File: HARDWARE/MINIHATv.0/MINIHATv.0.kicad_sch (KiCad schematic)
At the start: 0 parts

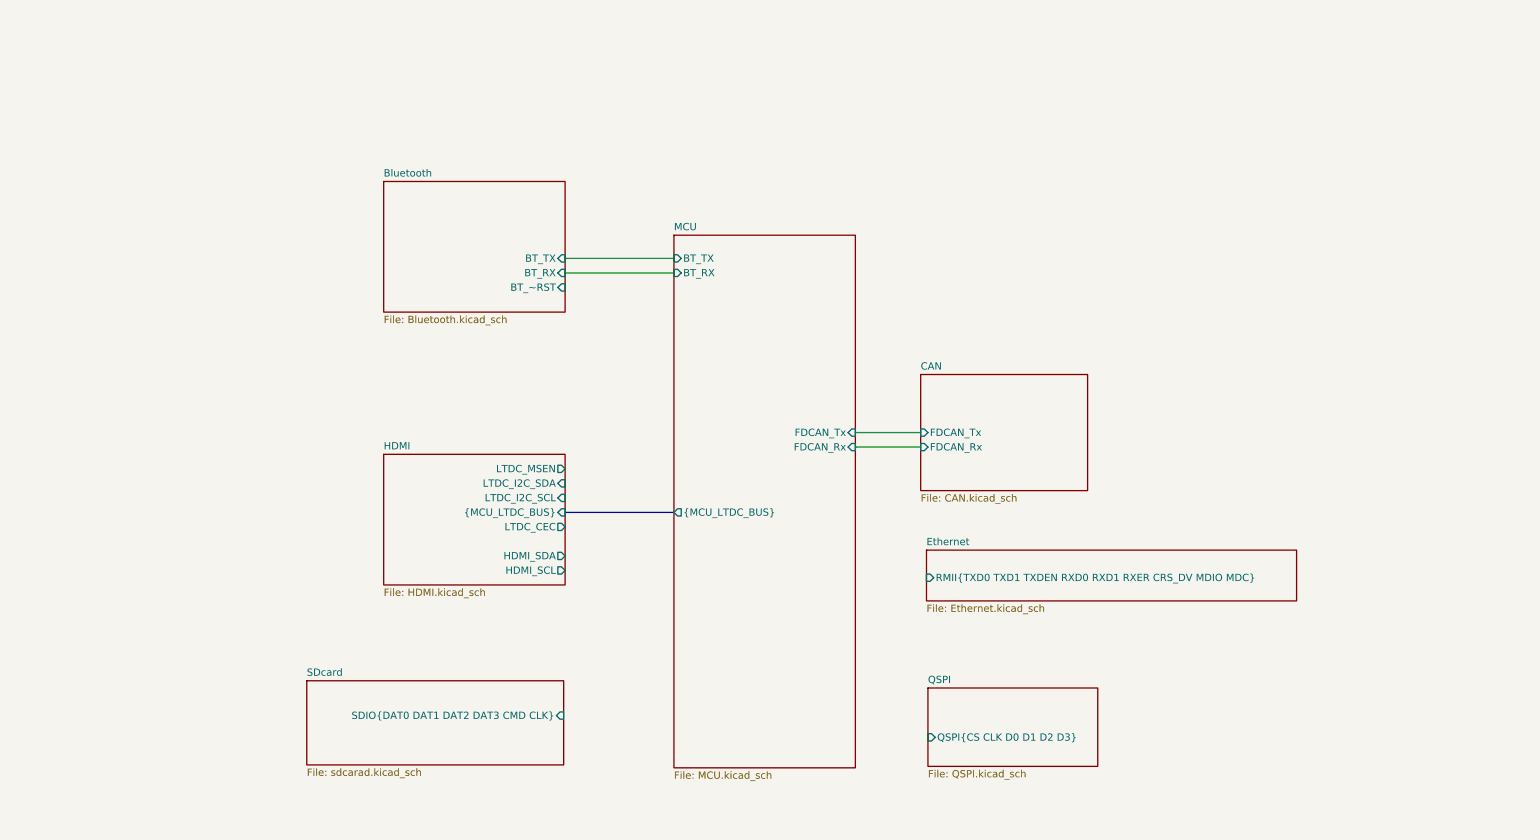
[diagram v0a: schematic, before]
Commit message: buses defined ind project settings, added stm antenna footprint, organized TOP
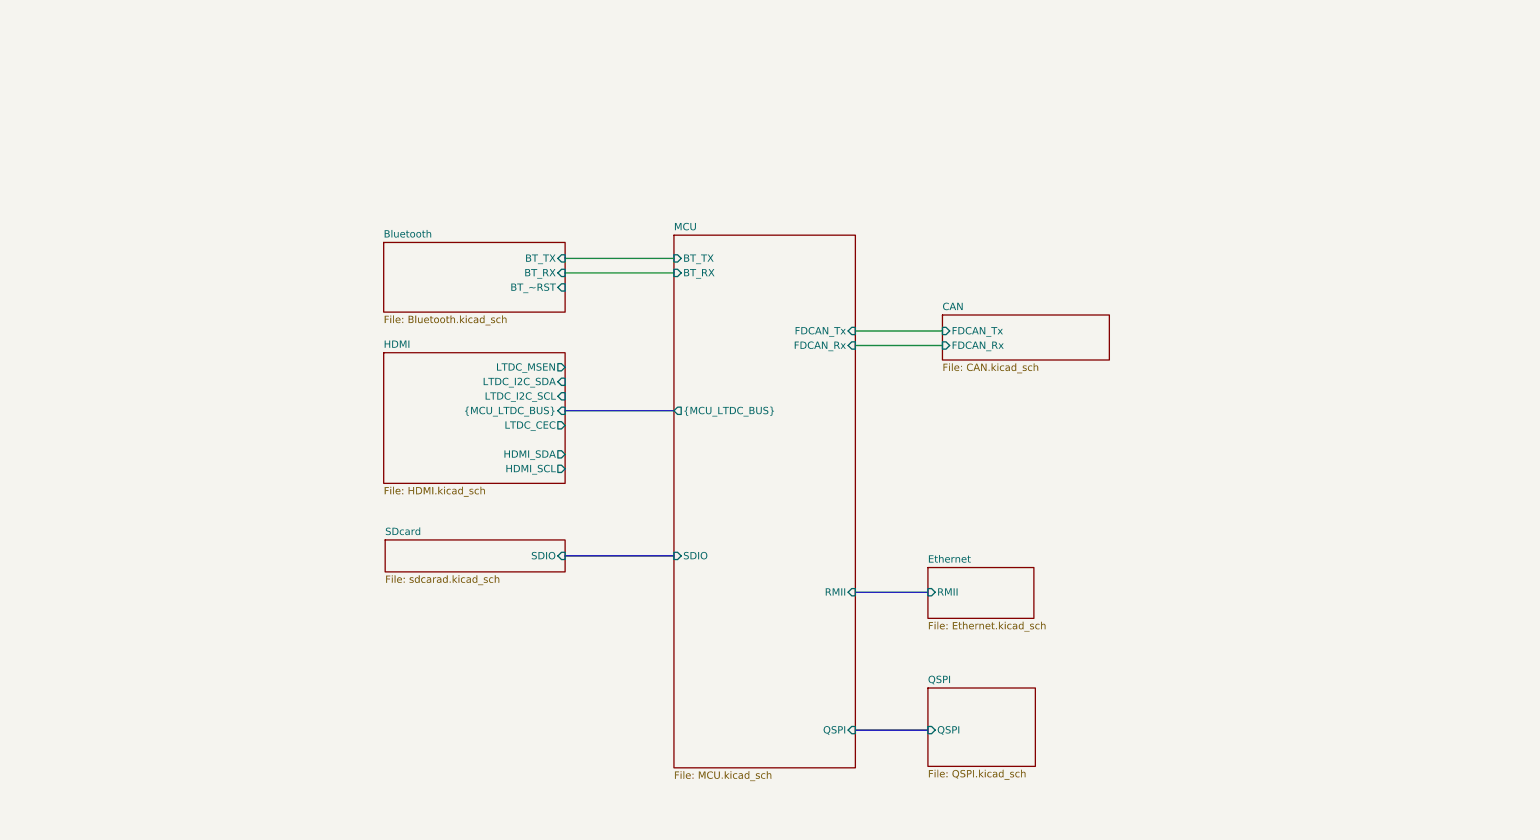
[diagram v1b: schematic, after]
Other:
- sheet Ethernet ports: added RMII; removed RMII{TXD0 TXD1 TXDEN RXD0 RXD1 RXER CRS_DV MDIO MDC}
- sheet MCU ports: added QSPI, RMII, SDIO; removed none
- sheet QSPI ports: added QSPI; removed QSPI{CS CLK D0 D1 D2 D3}
- sheet SDcard ports: added SDIO; removed SDIO{DAT0 DAT1 DAT2 DAT3 CMD CLK}
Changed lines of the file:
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@@
 	(wire
 		(pts
-			(xy 160.02 86.36) (xy 171.45 86.36)
+			(xy 160.02 68.58) (xy 175.26 68.58)
+		)
+		(stroke
+			(width 0)
+			(type default)
+		)
+	)
+	(bus
+		(pts
+			(xy 160.02 138.43) (xy 172.72 138.43)
 		)
 		(stroke
@@
 		)
 	)
+	(bus
+		(pts
+			(xy 109.22 107.95) (xy 128.27 107.95)
+		)
+		(stroke
+			(width 0)
+			(type default)
+		)
+	)
 	(wire
 		(pts
-			(xy 160.02 88.9) (xy 171.45 88.9)
+			(xy 160.02 71.12) (xy 175.26 71.12)
 		)
 		(stroke
@@
 	(bus
 		(pts
-			(xy 109.22 100.33) (xy 128.27 100.33)
-		)
-		(stroke
-			(width 0)
-			(type default)
-		)
-	)
-	(sheet
-		(at 77.47 42.418)
-		(size 31.75 22.86)
+			(xy 109.22 82.55) (xy 128.27 82.55)
+		)
+		(stroke
+			(width 0)
+			(type default)
+		)
+	)
+	(bus
+		(pts
+			(xy 160.02 114.3) (xy 172.72 114.3)
+		)
+		(stroke
+			(width 0)
+			(type default)
+		)
+	)
+	(sheet
+		(at 77.47 53.086)
+		(size 31.75 12.192)
 		(exclude_from_sim no)
 		(in_bom yes)
@@
 		)
 		(property "Sheetname" "Bluetooth"
-			(at 77.47 41.7064 0)
+			(at 77.47 52.3744 0)
 			(show_name no)
 			(do_not_autoplace no)
@@
 	)
 	(sheet
-		(at 171.45 76.2)
-		(size 29.21 20.32)
+		(at 175.26 65.786)
+		(size 29.21 7.874)
 		(exclude_from_sim no)
 		(in_bom yes)
@@
 		)
 		(property "Sheetname" "CAN"
-			(at 171.45 75.4884 0)
+			(at 175.26 65.0744 0)
 			(show_name no)
 			(do_not_autoplace no)
@@
 		)
 		(property "Sheetfile" "CAN.kicad_sch"
-			(at 171.45 97.1046 0)
+			(at 175.26 74.2446 0)
 			(show_name no)
 			(do_not_autoplace no)
@@
 		)
 		(pin "FDCAN_Rx" input
-			(at 171.45 88.9 180)
+			(at 175.26 71.12 180)
 			(effects
 				(font
@@
 		)
 		(pin "FDCAN_Tx" input
-			(at 171.45 86.36 180)
+			(at 175.26 68.58 180)
 			(effects
 				(font
@@
 	)
 	(sheet
-		(at 77.47 90.17)
+		(at 77.47 72.39)
 		(size 31.75 22.86)
 		(exclude_from_sim no)
@@
 		)
 		(property "Sheetname" "HDMI"
-			(at 77.47 89.4584 0)
+			(at 77.47 71.6784 0)
 			(show_name no)
 			(do_not_autoplace no)
@@
 		)
 		(property "Sheetfile" "HDMI.kicad_sch"
-			(at 77.47 113.6146 0)
+			(at 77.47 95.8346 0)
 			(show_name no)
 			(do_not_autoplace no)
@@
 		)
 		(pin "{MCU_LTDC_BUS}" input
-			(at 109.22 100.33 0)
+			(at 109.22 82.55 0)
 			(effects
 				(font
@@
 		)
 		(pin "HDMI_SCL" output
-			(at 109.22 110.49 0)
+			(at 109.22 92.71 0)
 			(effects
 				(font
@@
 		)
 		(pin "HDMI_SDA" output
-			(at 109.22 107.95 0)
+			(at 109.22 90.17 0)
 			(effects
 				(font
@@
 		)
 		(pin "LTDC_CEC" output
-			(at 109.22 102.87 0)
+			(at 109.22 85.09 0)
 			(effects
 				(font
@@
 		)
 		(pin "LTDC_I2C_SCL" input
-			(at 109.22 97.79 0)
+			(at 109.22 80.01 0)
 			(effects
 				(font
@@
 		)
 		(pin "LTDC_I2C_SDA" input
-			(at 109.22 95.25 0)
+			(at 109.22 77.47 0)
 			(effects
 				(font
@@
 		)
 		(pin "LTDC_MSEN" output
-			(at 109.22 92.71 0)
+			(at 109.22 74.93 0)
 			(effects
 				(font
@@
 	)
 	(sheet
-		(at 172.466 106.934)
-		(size 64.77 8.89)
+		(at 172.72 109.982)
+		(size 18.542 8.89)
 		(exclude_from_sim no)
 		(in_bom yes)
@@
 		)
 		(property "Sheetname" "Ethernet"
-			(at 172.466 106.2224 0)
+			(at 172.72 109.2704 0)
 			(show_name no)
 			(do_not_autoplace no)
@@
 		)
 		(property "Sheetfile" "Ethernet.kicad_sch"
-			(at 172.466 116.4086 0)
-			(show_name no)
-			(do_not_autoplace no)
-			(effects
-				(font
-					(size 1.27 1.27)
-				)
-				(justify left top)
-			)
-		)
-		(pin "RMII{TXD0 TXD1 TXDEN RXD0 RXD1 RXER CRS_DV MDIO MDC}" input
-			(at 172.466 111.76 180)
+			(at 172.72 119.4566 0)
+			(show_name no)
+			(do_not_autoplace no)
+			(effects
+				(font
+					(size 1.27 1.27)
+				)
+				(justify left top)
+			)
+		)
+		(pin "RMII" input
+			(at 172.72 114.3 180)
 			(effects
 				(font
@@
 	)
 	(sheet
-		(at 64.008 129.794)
-		(size 44.958 14.732)
+		(at 77.724 105.156)
+		(size 31.496 5.588)
 		(exclude_from_sim no)
 		(in_bom yes)
@@
 		)
 		(property "Sheetname" "SDcard"
-			(at 64.008 129.0824 0)
+			(at 77.724 104.4444 0)
 			(show_name no)
 			(do_not_autoplace no)
@@
 		)
 		(property "Sheetfile" "sdcarad.kicad_sch"
-			(at 64.008 145.1106 0)
-			(show_name no)
-			(do_not_autoplace no)
-			(effects
-				(font
-					(size 1.27 1.27)
-				)
-				(justify left top)
-			)
-		)
-		(pin "SDIO{DAT0 DAT1 DAT2 DAT3 CMD CLK}" input
-			(at 108.966 135.89 0)
+			(at 77.724 111.3286 0)
+			(show_name no)
+			(do_not_autoplace no)
+			(effects
+				(font
+					(size 1.27 1.27)
+				)
+				(justify left top)
+			)
+		)
+		(pin "SDIO" input
+			(at 109.22 107.95 0)
 			(effects
 				(font
@@
 		)
 		(pin "FDCAN_Rx" input
-			(at 160.02 88.9 0)
+			(at 160.02 71.12 0)
 			(effects
 				(font
@@
 		)
 		(pin "FDCAN_Tx" input
-			(at 160.02 86.36 0)
+			(at 160.02 68.58 0)
 			(effects
 				(font
@@
 		)
 		(pin "{MCU_LTDC_BUS}" output
-			(at 128.27 100.33 180)
+			(at 128.27 82.55 180)
 			(effects
 				(font
@@
 		(pin "BT_TX" input
 			(at 128.27 55.88 180)
+			(effects
+				(font
+					(size 1.27 1.27)
+				)
+				(justify left)
+			)
+		)
+		(pin "QSPI" input
+			(at 160.02 138.43 0)
+			(effects
+				(font
+					(size 1.27 1.27)
+				)
+				(justify right)
+			)
+		)
+		(pin "RMII" input
+			(at 160.02 114.3 0)
+			(effects
+				(font
+					(size 1.27 1.27)
+				)
+				(justify right)
+			)
+		)
+		(pin "SDIO" input
+			(at 128.27 107.95 180)
 			(effects
 				(font
@@
 	(sheet
 		(at 172.72 131.064)
-		(size 29.718 13.716)
+		(size 18.796 13.716)
 		(exclude_from_sim no)
 		(in_bom yes)
@@
 			)
 		)
-		(pin "QSPI{CS CLK D0 D1 D2 D3}" input
-			(at 172.72 139.7 180)
-			(effects
-				(font
+		(pin "QSPI" input
+			(at 172.72 138.43 180)
+			(effects
+				(font

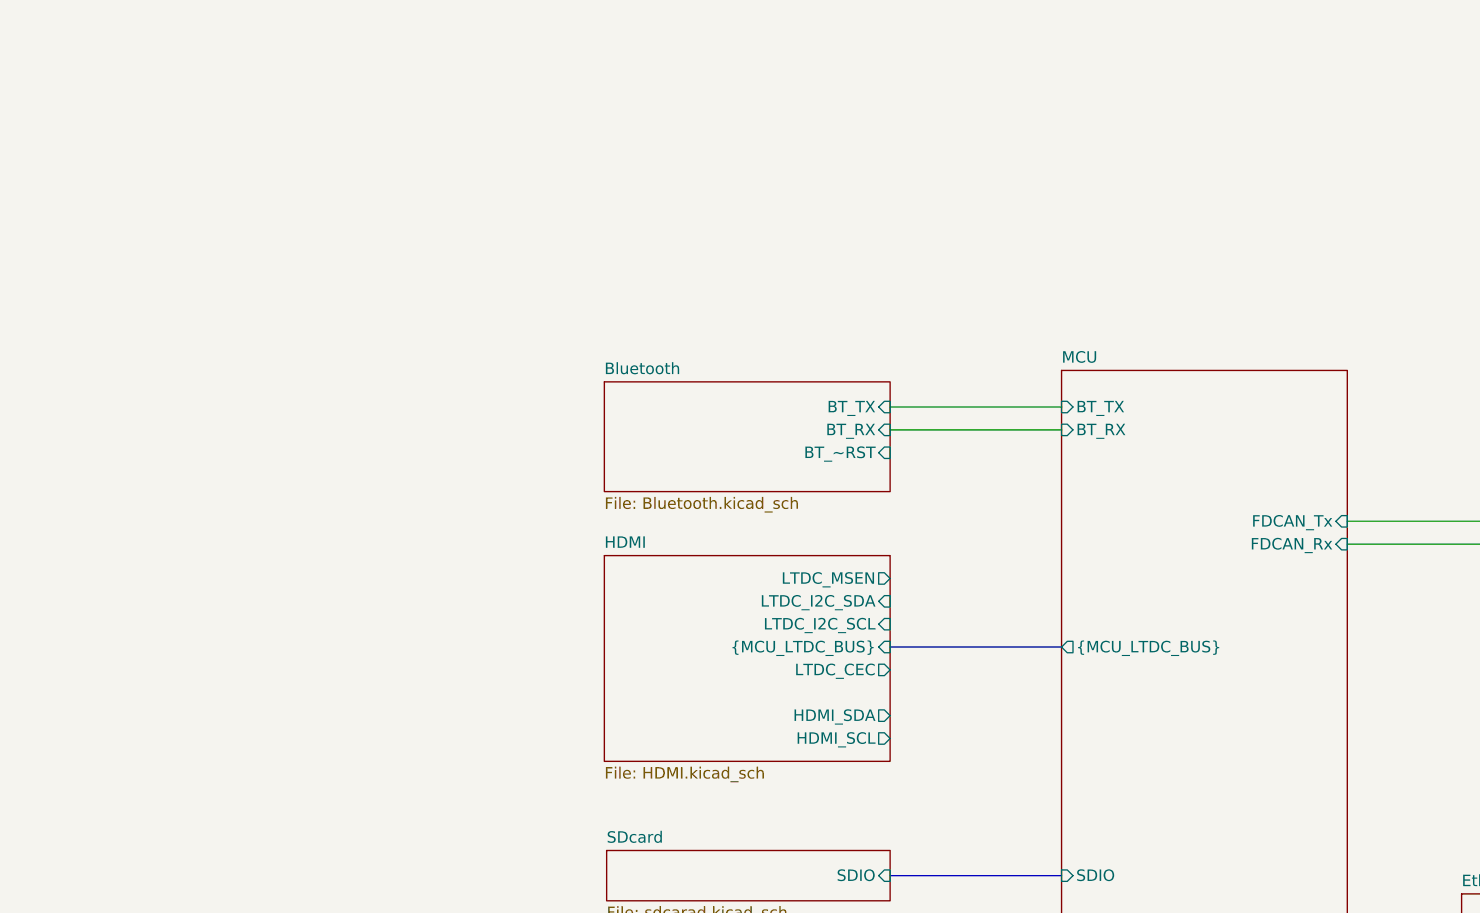
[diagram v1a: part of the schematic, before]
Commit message: added i2c for hdmi
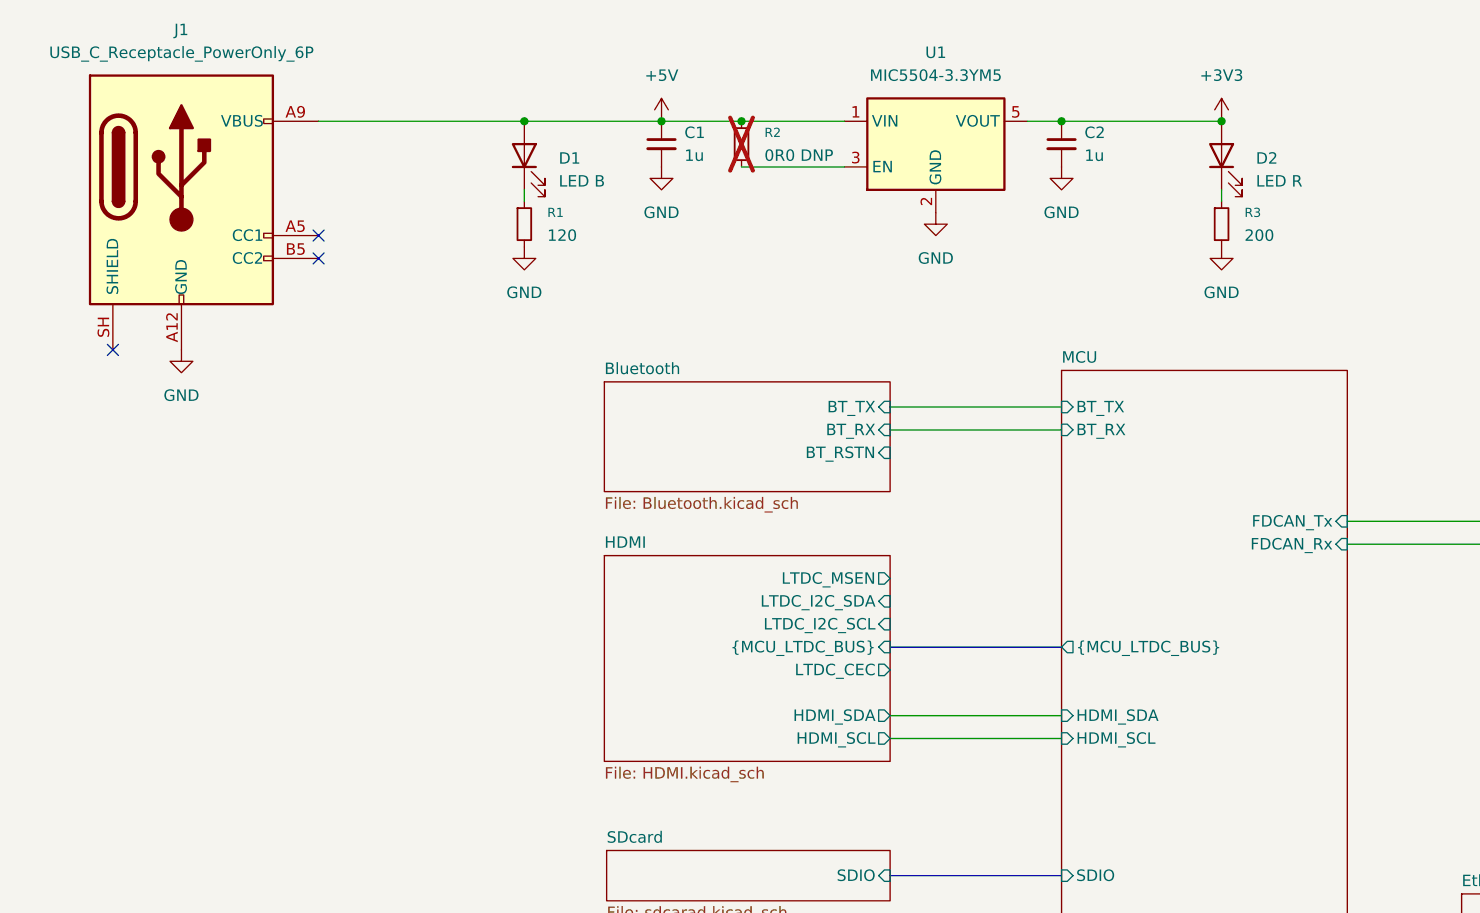
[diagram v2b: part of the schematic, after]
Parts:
- added C1, C2: 1u, symbol Device:C_Small
- added D1: LED B, symbol Device:LED
- added D2: LED R, symbol Device:LED
- added J1: USB_C_Receptacle_PowerOnly_6P, symbol Connector:USB_C_Receptacle_PowerOnly_6P
- added R1: 120, symbol Device:R_Small
- added R2: 0R0 DNP, symbol Device:R_Small
- added R3: 200, symbol Device:R_Small
- added U1: MIC5504-3.3YM5, Package_TO_SOT_SMD:SOT-23-5, symbol Regulator_Linear:MIC5504-3.3YM5
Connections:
- new net: R2.1, U1.3 (EN)
- new net: D1.1 (K), R1.1
- new net: D2.1 (K), R3.1
- new net +3V3: C2.1, D2.2 (A), U1.5 (VOUT)
- new net +5V: C1.1, D1.2 (A), J1.A9 (VBUS), J1.B9 (VBUS), R2.2, U1.1 (VIN)
- new net GND: C1.2, C2.2, J1.A12 (GND), J1.B12 (GND), R1.2, R3.2, U1.2 (GND)
- no-connect marks 0 -> 3
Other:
- sheet Bluetooth ports: added BT_RSTN; removed BT_~RST
- sheet MCU ports: added HDMI_SCL, HDMI_SDA; removed none
